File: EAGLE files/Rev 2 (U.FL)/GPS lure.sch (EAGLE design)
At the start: 8 parts, among them J1 U.FL

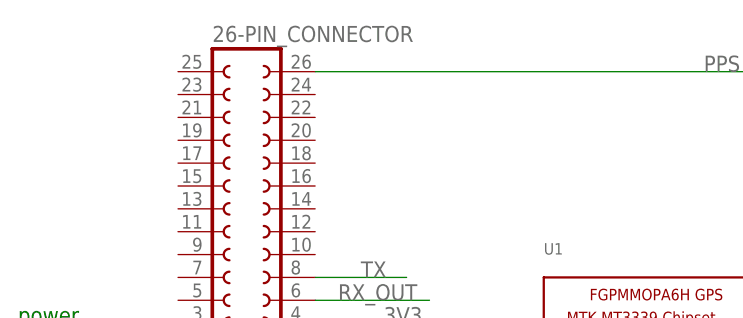
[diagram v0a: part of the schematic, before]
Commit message: Updated Eagle Files to make silkscreen cleaner
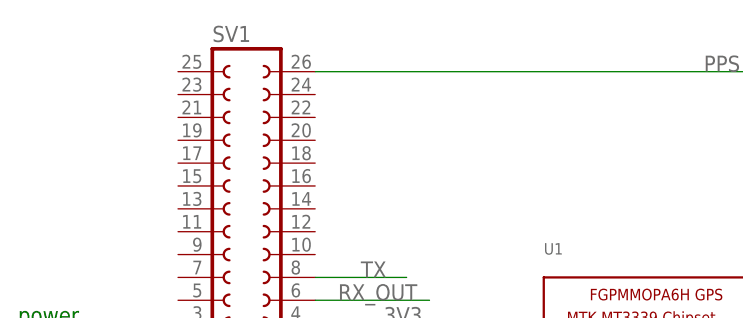
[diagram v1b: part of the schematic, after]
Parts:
- removed 26-PIN_CONNECTOR: (no value), con-lsta:FE13-2W
- added SV1: (no value), con-lsta:FE13-2
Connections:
- net 3V3: now also SV1.4; no longer 26-PIN_CONNECTOR.4
- net GND: now also SV1.1; no longer 26-PIN_CONNECTOR.1
- net PPS: now also SV1.26; no longer 26-PIN_CONNECTOR.26
- net RX_OUT: now also SV1.6; no longer 26-PIN_CONNECTOR.6
- net TX: now also SV1.8; no longer 26-PIN_CONNECTOR.8
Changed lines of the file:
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@@
 </classes>
 <parts>
-<part name="26-PIN_CONNECTOR" library="con-lsta" deviceset="FE13-2W" device=""/>
 <part name="U1" library="adafruit" deviceset="GPS_FGPMMOPA6H" device=""/>
 <part name="D1" library="diode" deviceset="DIODE-" device="SOD123" value="1N4148"/>
@@
 <part name="LED2" library="led" deviceset="LED" device="CHIPLED_1206" value="Red"/>
 <part name="J1" library="SparkFun-Connectors" deviceset="U.FL" device="" value="U.FL"/>
+<part name="SV1" library="con-lsta" deviceset="FE13-2" device=""/>
 </parts>
 <sheets>
@@
 </plain>
 <instances>
-<instance part="26-PIN_CONNECTOR" gate="1" x="68.58" y="55.88"/>
 <instance part="U1" gate="G$1" x="114.3" y="27.94"/>
 <instance part="D1" gate="G$1" x="76.2" y="15.24" rot="R180"/>
@@
 <instance part="LED2" gate="G$1" x="93.98" y="27.94" rot="R270"/>
 <instance part="J1" gate="G$1" x="137.16" y="10.16" rot="R90"/>
+<instance part="SV1" gate="G$1" x="68.58" y="55.88"/>
 </instances>
 <busses>
@@
 <net name="GND" class="0">
 <segment>
-<pinref part="26-PIN_CONNECTOR" gate="1" pin="1"/>
 <wire x1="60.96" y1="40.64" x2="60.96" y2="35.56" width="0.1524" layer="91"/>
 <wire x1="60.96" y1="35.56" x2="60.96" y2="33.02" width="0.1524" layer="91"/>
@@
 <pinref part="R4" gate="G$1" pin="2"/>
 <pinref part="C1" gate="G$1" pin="2"/>
+<pinref part="SV1" gate="G$1" pin="1"/>
 </segment>
 <segment>
@@
 <net name="3V3" class="0">
 <segment>
-<pinref part="26-PIN_CONNECTOR" gate="1" pin="4"/>
 <wire x1="76.2" y1="43.18" x2="81.28" y2="43.18" width="0.1524" layer="91"/>
 <wire x1="81.28" y1="43.18" x2="91.44" y2="43.18" width="0.1524" layer="91"/>
@@
 <pinref part="C1" gate="G$1" pin="1"/>
 <junction x="81.28" y="43.18"/>
+<pinref part="SV1" gate="G$1" pin="4"/>
 </segment>
 <segment>
@@
 <wire x1="129.54" y1="20.32" x2="142.24" y2="20.32" width="0.1524" layer="91"/>
 <wire x1="142.24" y1="20.32" x2="142.24" y2="71.12" width="0.1524" layer="91"/>
-<pinref part="26-PIN_CONNECTOR" gate="1" pin="26"/>
 <wire x1="76.2" y1="71.12" x2="142.24" y2="71.12" width="0.1524" layer="91"/>
 <label x="119.38" y="71.12" size="1.778" layer="95"/>
+<pinref part="SV1" gate="G$1" pin="26"/>
 </segment>
 </net>
@@
 </segment>
 <segment>
-<pinref part="26-PIN_CONNECTOR" gate="1" pin="8"/>
 <wire x1="76.2" y1="48.26" x2="86.36" y2="48.26" width="0.1524" layer="91"/>
 <label x="81.28" y="48.26" size="1.778" layer="95"/>
+<pinref part="SV1" gate="G$1" pin="8"/>
 </segment>
 </net>
@@
 </segment>
 <segment>
-<pinref part="26-PIN_CONNECTOR" gate="1" pin="6"/>
 <wire x1="76.2" y1="45.72" x2="88.9" y2="45.72" width="0.1524" layer="91"/>
 <label x="78.74" y="45.72" size="1.778" layer="95"/>
+<pinref part="SV1" gate="G$1" pin="6"/>
 </segment>
 </net>
